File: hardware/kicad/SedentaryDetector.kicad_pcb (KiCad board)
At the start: 2 copper layers, 2 parts, among them J1 ESP32_2x15, J2 MPU6050_1x8

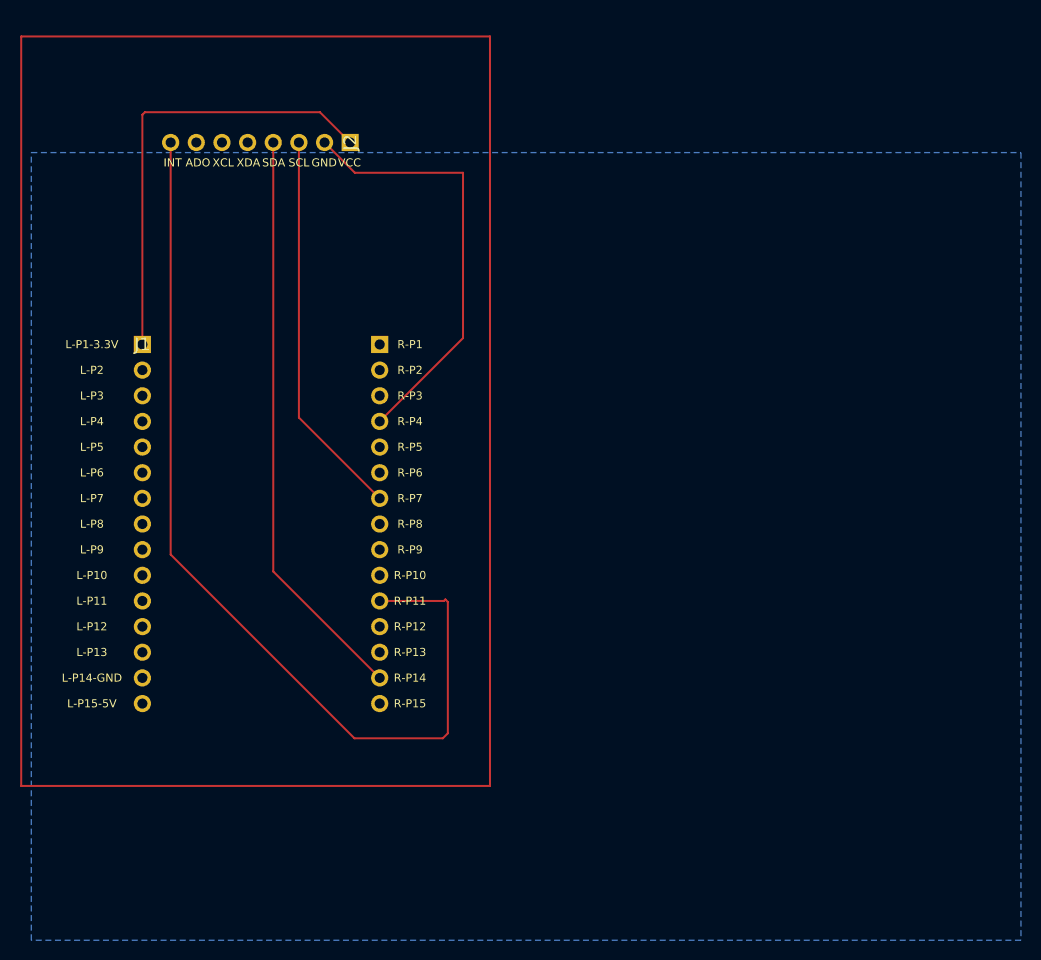
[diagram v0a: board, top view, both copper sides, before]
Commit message: V0.3: PCB layout ready for routing
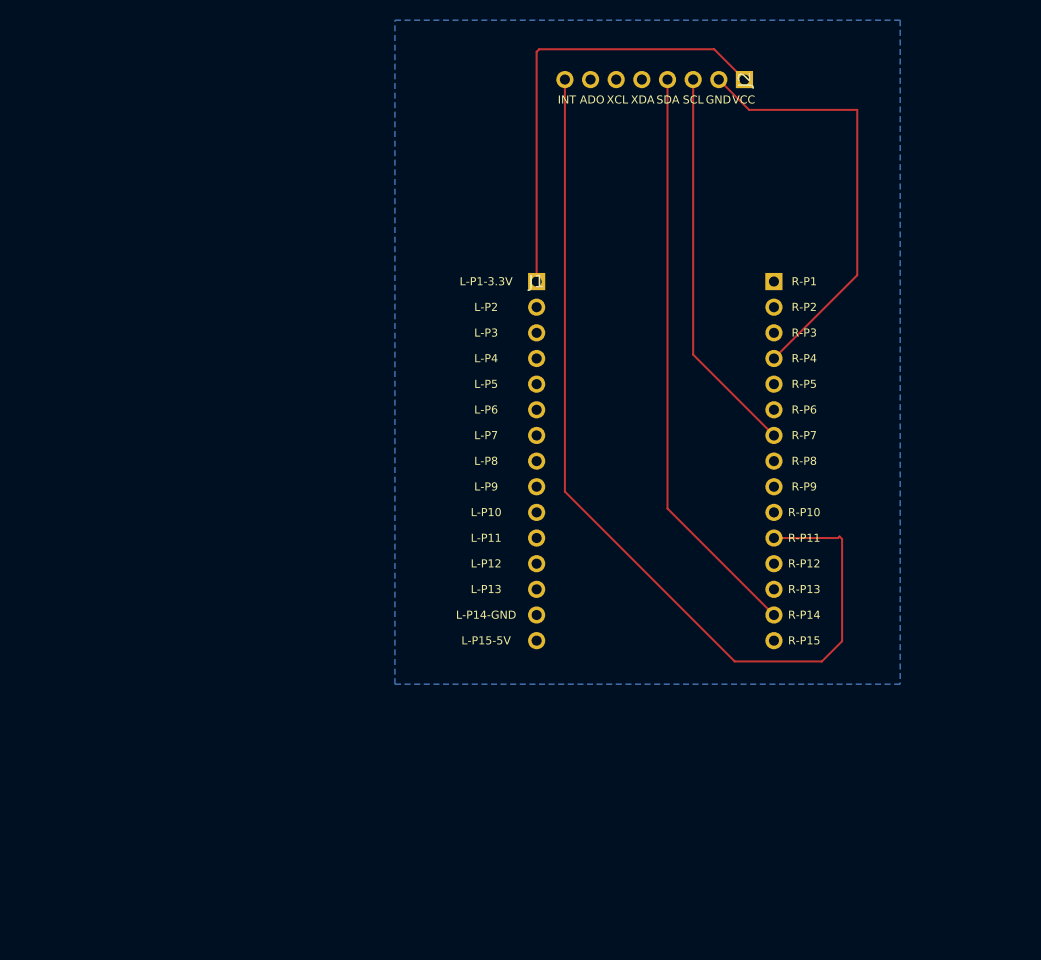
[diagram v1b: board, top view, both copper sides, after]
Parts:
- moved J1 39.5 mm to (149.5, 78.8)
- moved J2 39.5 mm to (170.1, 58.8)
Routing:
- net MPU_INT: track 95.9 -> 93.1 mm

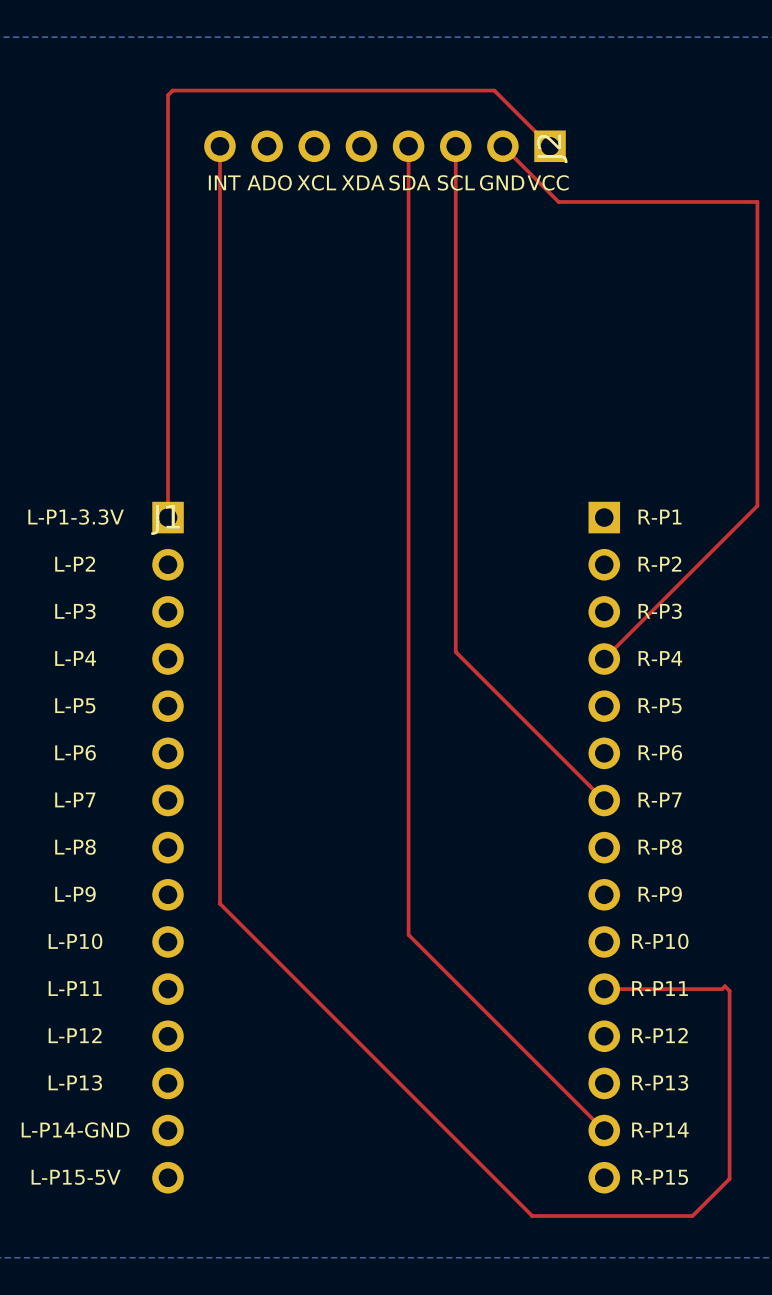
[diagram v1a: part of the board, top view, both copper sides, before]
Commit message: feat(hardware): add tight Edge.Cuts border 30x62mm
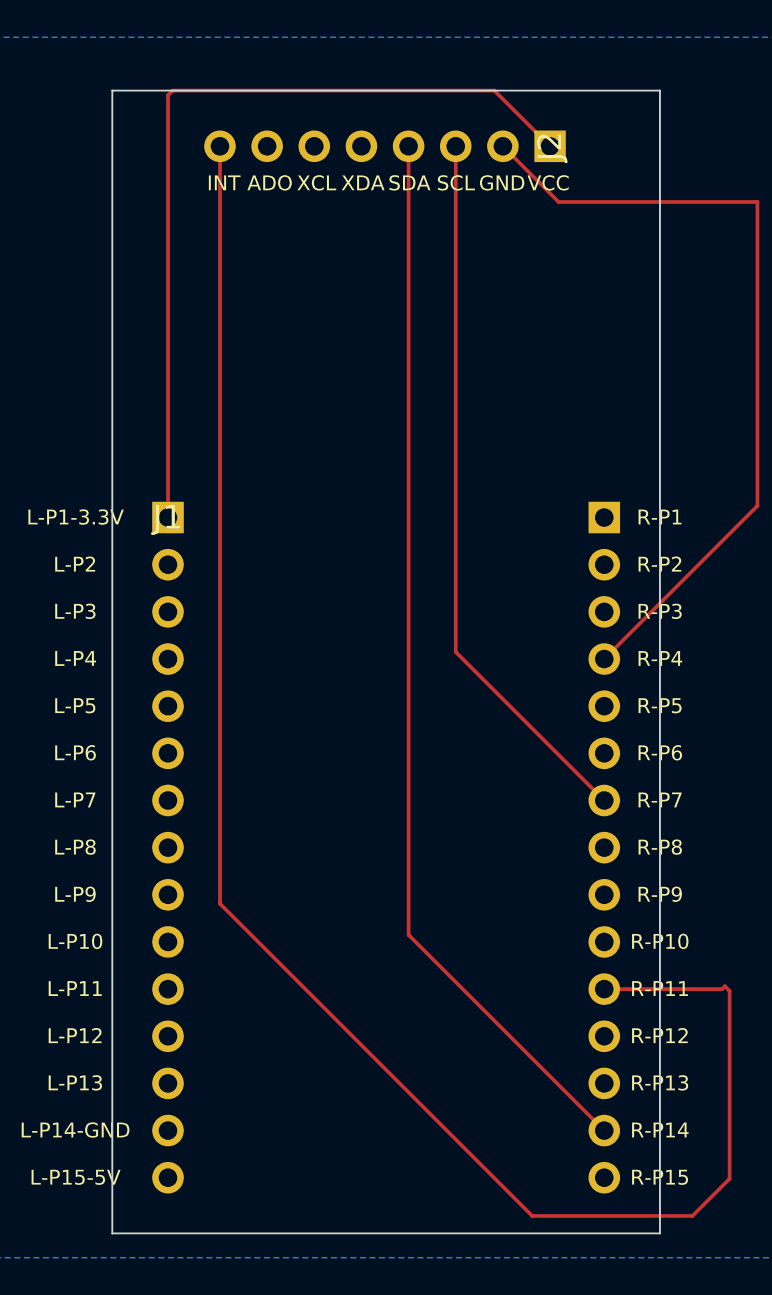
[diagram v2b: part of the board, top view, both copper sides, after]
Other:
- board outline added: 29.5 x 61.6 mm
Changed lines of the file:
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@@
 		(embedded_fonts no)
+	)
+	(gr_line
+		(start 146.54 55.77)
+		(end 176.04 55.77)
+		(stroke
+			(width 0.1)
+			(type default)
+		)
+		(layer "Edge.Cuts")
+	)
+	(gr_line
+		(start 146.54 117.33)
+		(end 146.54 55.77)
+		(stroke
+			(width 0.1)
+			(type default)
+		)
+		(layer "Edge.Cuts")
+	)
+	(gr_line
+		(start 176.04 55.77)
+		(end 176.04 117.33)
+		(stroke
+			(width 0.1)
+			(type default)
+		)
+		(layer "Edge.Cuts")
+	)
+	(gr_line
+		(start 176.04 117.33)
+		(end 146.54 117.33)
+		(stroke
+			(width 0.1)
+			(type default)
+		)
+		(layer "Edge.Cuts")
 	)
 	(gr_text "L-P14-GND\n"
